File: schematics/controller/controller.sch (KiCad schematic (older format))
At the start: 11 parts, among them J1001 Screw_Terminal_01x03, J1002 Screw_Terminal_01x03, J1003 Conn_01x02_Male, J1004 Conn_01x04_Male, J1005 Screw_Terminal_01x02, J1006 Screw_Terminal_01x02, J1007 Conn_01x04_Male, J1008 Screw_Terminal_01x02, J1009 FRONTPANEL, J1010 Screw_Terminal_01x02, U1001 Module: surgeprot.mains.275.5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

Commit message: Redesign, signalling.
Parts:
- added J1010: SENS_INSIDE, symbol Screw_Terminal_01x02
- added J1011: SENS_OUTSIDE, symbol Screw_Terminal_01x02
- J1005: value Screw_Terminal_01x02 -> SENS_INSIDE
- J1006: value Screw_Terminal_01x02 -> SENS_OUTSIDE
- J1008: value Screw_Terminal_01x02 -> HEAT_VALVE
- J1012: renamed from J1010; value Screw_Terminal_01x02 -> HEAT_VALVE
- U1001: footprint (none) -> fan-controller_parts:MOV_Surge_Protector
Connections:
- net comms/SIG_X_OUT: now also J1010.1 (Pin_1), J1011.1 (Pin_1)
- net comms/SIG_Y_OUT: now also J1010.2 (Pin_2), J1011.2 (Pin_2)
- net cpu/SCL_HIBAUD renamed cpu/CPU_HIBAUD_SCL
- net cpu/SDA_HIBAUD renamed cpu/CPU_HIBAUD_SDA
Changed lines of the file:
@@
 $Descr A3 16535 11693
 encoding utf-8
-Sheet 1 21
+Sheet 1 19
 Title "Controller"
 Date "2017-09-24"
@@
 F 0 "U1001" H 3950 2450 60  0000 C CNN
 F 1 "Module: surgeprot.mains.275.5.01" H 3950 2350 39  0000 C CNN
-F 2 "" H 3950 1800 60  0000 C CNN
+F 2 "fan-controller_parts:MOV_Surge_Protector" H 3950 1500 60  0001 C CNN
 F 3 "" H 3950 1800 60  0000 C CNN
 	1    3950 2150
@@
 F3 "GND" I L 9550 9250 60
 F4 "VEE" I L 9550 9350 60
-F5 "UNMUTE_15K" I L 9550 8450 60
-F6 "UNMUTE_25K" I L 9550 8550 60
-F7 "OUT_15K_PRESENT" O R 11800 8450 60
-F8 "OUT_25K_PRESENT" O R 11800 8550 60
-F9 "EARTH" U L 9550 8950 60
-F10 "SIG_X_OUT" B R 11800 9250 60
-F11 "SIG_Y_OUT" B R 11800 9350 60
+F5 "OSC_15K_UNMUTE_10BAUD_SDA" I L 9550 8450 60
+F6 "OSC_25K_UNMUTE_10BAUD_SCL" I L 9550 8550 60
+F7 "EARTH" U L 9550 8950 60
+F8 "SIG_X_OUT" B R 11800 9250 60
+F9 "SIG_Y_OUT" B R 11800 9350 60
+F10 "DETECTOR_15K_10BAUD_SDA" O R 11800 8750 60
 $EndSheet
 $Comp
-L Screw_Terminal_01x02 J1010
+L Screw_Terminal_01x02 J1012
 U 1 1 5A4979A3
 P 15150 9250
-F 0 "J1010" H 15150 9350 50  0000 C CNN
-F 1 "Screw_Terminal_01x02" H 15150 9050 50  0001 C CNN
+F 0 "J1012" H 15150 9350 50  0000 C CNN
+F 1 "HEAT_VALVE" H 15350 9200 50  0000 L CNN
 F 2 "" H 15150 9250 50  0001 C CNN
 F 3 "" H 15150 9250 50  0001 C CNN
@@
 P 15150 3300
 F 0 "J1005" H 15150 3400 50  0000 C CNN
-F 1 "Screw_Terminal_01x02" H 15150 3100 50  0001 C CNN
+F 1 "SENS_INSIDE" H 15350 3250 50  0000 L CNN
 F 2 "" H 15150 3300 50  0001 C CNN
 F 3 "" H 15150 3300 50  0001 C CNN
@@
 P 15150 3650
 F 0 "J1006" H 15150 3750 50  0000 C CNN
-F 1 "Screw_Terminal_01x02" H 15150 3450 50  0001 C CNN
+F 1 "SENS_OUTSIDE" H 15350 3600 50  0000 L CNN
 F 2 "" H 15150 3650 50  0001 C CNN
 F 3 "" H 15150 3650 50  0001 C CNN
@@
 P 15150 4000
 F 0 "J1008" H 15150 4100 50  0000 C CNN
-F 1 "Screw_Terminal_01x02" H 15150 3800 50  0001 C CNN
+F 1 "HEAT_VALVE" H 15350 3950 50  0000 L CNN
 F 2 "" H 15150 4000 50  0001 C CNN
 F 3 "" H 15150 4000 50  0001 C CNN
@@
 F2 "V_LOGIC" U L 9550 5750 60
 F3 "GND" U L 9550 5850 60
-F4 "SDA_10" B R 11800 5450 60
-F5 "SCL_10" B R 11800 5550 60
-F6 "SDA_HIBAUD" B R 11800 5050 60
-F7 "SCL_HIBAUD" B R 11800 5150 60
+F4 "CPU_10BAUD_SDA" B R 11800 5450 60
+F5 "CPU_10BAUD_SCL" O R 11800 5550 60
+F6 "CPU_HIBAUD_SDA" B R 11800 5050 60
+F7 "CPU_HIBAUD_SCL" O R 11800 5150 60
 F8 "RESET" I R 11800 5250 60
-F9 "WR_EN" O R 11800 5650 60
+F9 "CPU_10BAUD_WR_EN" O R 11800 5650 60
 F10 "FAN_ON" O R 11800 4950 60
-$EndSheet
-$Sheet
-S 9550 6600 2250 1100
-U 5A9355B1
-F0 "comms_router" 60
-F1 "sub_assy/comms/router.sch" 60
-F2 "SCL" B R 11800 6750 60
-F3 "SDA" B R 11800 6650 60
-F4 "WR_EN" I R 11800 6850 60
-F5 "DETECTOR_15K" I R 11800 7100 60
-F6 "DETECTOR_25K" I R 11800 7200 60
-F7 "UNMUTE_15K" O L 9550 7100 60
-F8 "UNMUTE_25K" O L 9550 7200 60
-F9 "V_LOGIC" U L 9550 7550 60
-F10 "GND" U L 9550 7650 60
 $EndSheet
 $Comp
@@
 P 15150 5050
 F 0 "J1009" H 15150 5350 50  0000 C CNN
-F 1 "FRONTPANEL" H 14750 5050 50  0000 C CNN
+F 1 "FRONTPANEL" H 14500 5050 50  0000 L CNN
 F 2 "" H 15150 5050 50  0001 C CNN
 F 3 "" H 15150 5050 50  0001 C CNN
@@
 Connection ~ 14300 3750
 Wire Wire Line
-	11800 7100 12250 7100
-Wire Wire Line
-	12250 7100 12250 8450
-Wire Wire Line
-	12250 8450 11800 8450
-Wire Wire Line
-	11800 7200 12150 7200
-Wire Wire Line
-	12150 7200 12150 8550
-Wire Wire Line
-	12150 8550 11800 8550
-Wire Wire Line
-	9550 7100 9050 7100
-Wire Wire Line
-	9050 7100 9050 8450
-Wire Wire Line
-	9050 8450 9550 8450
-Wire Wire Line
-	9550 7200 9200 7200
-Wire Wire Line
-	9200 7200 9200 8550
-Wire Wire Line
-	9200 8550 9550 8550
-Wire Wire Line
 	5500 4500 14400 4500
 Wire Wire Line
@@
 	11800 5250 14950 5250
 Wire Wire Line
-	11800 5450 12250 5450
-Wire Wire Line
-	12250 5450 12250 6650
-Wire Wire Line
-	12250 6650 11800 6650
-Wire Wire Line
-	11800 5550 12150 5550
-Wire Wire Line
-	12150 5550 12150 6750
-Wire Wire Line
-	12150 6750 11800 6750
-Wire Wire Line
-	11800 5650 12050 5650
-Wire Wire Line
-	12050 5650 12050 6850
-Wire Wire Line
-	12050 6850 11800 6850
-Wire Wire Line
 	1700 10500 1700 10300
+$Sheet
+S 9550 6600 2250 1100
+U 5A9355B1
+F0 "comms_router" 60
+F1 "sub_assy/comms/router.sch" 60
+F2 "V_LOGIC" U L 9550 7550 60
+F3 "GND" U L 9550 7650 60
+F4 "OSC_25K_UNMUTE_10BAUD_SCL" O L 9550 6750 60
+F5 "CPU_10BAUD_SCL" I R 11800 7100 60
+F6 "CPU_10BAUD_WR_EN" I R 11800 7200 60
+F7 "DETECTOR_15K_10BAUD_SDA" I R 11800 7550 60
+F8 "OSC_15K_UNMUTE_10BAUD_SDA" O L 9550 6650 60
+F9 "CPU_10BAUD_SDA" B R 11800 7000 60
+$EndSheet
+Wire Wire Line
+	11800 5450 12200 5450
+Wire Wire Line
+	11800 5550 12300 5550
+Wire Wire Line
+	11800 5650 12400 5650
+Wire Wire Line
+	9300 8450 9550 8450
+Wire Wire Line
+	9200 8550 9550 8550
+Wire Wire Line
+	12400 5650 12400 7200
+Wire Wire Line
+	12400 7200 11800 7200
+Wire Wire Line
+	12300 5550 12300 7100
+Wire Wire Line
+	12300 7100 11800 7100
+Wire Wire Line
+	12200 5450 12200 7000
+Wire Wire Line
+	12200 7000 11800 7000
+Wire Wire Line
+	9550 6650 9300 6650
+Wire Wire Line
+	9300 6650 9300 8450
+Wire Wire Line
+	9550 6750 9200 6750
+Wire Wire Line
+	9200 6750 9200 8550
+Wire Wire Line
+	11800 8750 12200 8750
+Wire Wire Line
+	12200 8750 12200 7550
+Wire Wire Line
+	12200 7550 11800 7550
+$Comp
+L Screw_Terminal_01x02 J1011
+U 1 1 5B48450F
+P 15150 8700
+F 0 "J1011" H 15150 8800 50  0000 C CNN
+F 1 "SENS_OUTSIDE" H 15350 8650 50  0000 L CNN
+F 2 "" H 15150 8700 50  0001 C CNN
+F 3 "" H 15150 8700 50  0001 C CNN
+	1    15150 8700
+	1    0    0    -1
+$EndComp
+$Comp
+L Screw_Terminal_01x02 J1010
+U 1 1 5B4846AD
+P 15150 8150
+F 0 "J1010" H 15150 8250 50  0000 C CNN
+F 1 "SENS_INSIDE" H 15350 8100 50  0000 L CNN
+F 2 "" H 15150 8150 50  0001 C CNN
+F 3 "" H 15150 8150 50  0001 C CNN
+	1    15150 8150
+	1    0    0    -1
+$EndComp
+Wire Wire Line
+	14300 9350 14300 8250
+Wire Wire Line
+	14300 8250 14950 8250
+Connection ~ 14300 9350
+Wire Wire Line
+	14400 9250 14400 8150
+Wire Wire Line
+	14400 8150 14950 8150
+Connection ~ 14400 9250
+Wire Wire Line
+	14950 8800 14300 8800
+Connection ~ 14300 8800
+Wire Wire Line
+	14950 8700 14400 8700
+Connection ~ 14400 8700
 $EndSCHEMATC

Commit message: Revisions and simplifications
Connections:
- net fan-switch/N: now also J1003.1 (Pin_1); no longer J1003.2 (Pin_2)
- net at U1001.3 (LProt): now also J1003.2 (Pin_2); no longer J1003.1 (Pin_1)
- net comms/SIG_X_OUT renamed comms/SIG_X_OUTSIDE
- net comms/SIG_Y_OUT renamed comms/SIG_Y_OUTSIDE
- net dcdc_surge-prot/V_DCDC_+18_OUT renamed psu/V_DCDC_+18
- net dcdc_surge-prot/V_DCDC_0_OUT renamed psu/V_DCDC_0
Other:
- moved on the sheet: J1003

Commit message: Diagram cleanup and corrections.
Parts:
- removed J1005, J1010: SENS_INSIDE, symbol Screw_Terminal_01x02
- removed J1006, J1011: SENS_OUTSIDE, symbol Screw_Terminal_01x02
- removed J1008, J1012: HEAT_VALVE, symbol Screw_Terminal_01x02
- added D1001, D1002, D1003, D1004, D1005, D1006, D1007, D1008, D1009: 1.5KE33CA, symbol D_TVS
- added D1010, D1011, D1012, D1013, D1014, D1015, D1016, D1017, D1018: 1.5KE30CA, symbol D_TVS
- added F1001, F1002, F1003, F1004, F1005, F1006: 250mAF, symbol Fuse
- added F1007, F1008, F1009, F1010, F1011, F1012: 100mAF, symbol Fuse
- added J1003: Periphery, symbol Screw_Terminal_01x12
- added R1001, R1002, R1003, R1004, R1005, R1006: 27Ω / 1W, symbol R
- added U1002, U1003, U1004: TDK T90-A75XSMD, symbol GDT-3
- renumbered J1003 to J1004, J1004 to J1005, J1007 to J1006, J1009 to J1007
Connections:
- net comms/GND is gone; now on net cpu/CPU_HIBAUD_SCL: J1007.1 (Pin_1)
- net Earth: now also J1007.5 (Pin_5), D1001.1 (A1), D1003.1 (A1), D1004.1 (A1), D1006.1 (A1), D1007.1 (A1), D1009.1 (A1), D1010.1 (A1), D1012.1 (A1), D1013.1 (A1), D1015.1 (A1), D1016.1 (A1), D1018.1 (A1), U1002.2, U1003.2, U1004.2
- net comms_router/V_LOGIC: now also J1007.4 (Pin_4); no longer J1007.2 (Pin_2)
- net cpu/CPU_HIBAUD_SCL: no longer J1007.4 (Pin_4)
- net cpu/CPU_HIBAUD_SDA: now also J1007.2 (Pin_2); no longer J1007.3 (Pin_3)
- net cpu/RESET: now also J1007.3 (Pin_3); no longer J1007.5 (Pin_5)
- net psu/V_DCDC_+18: now also D1001.2 (A2), D1002.2 (A2), D1004.2 (A2), D1005.2 (A2), D1007.2 (A2), D1008.2 (A2), F1001.1, F1003.1, F1005.1
- net psu/V_DCDC_0: now also D1002.1 (A1), D1003.2 (A2), D1005.1 (A1), D1006.2 (A2), D1008.1 (A1), D1009.2 (A2), F1002.1, F1004.1, F1006.1
- new net: F1001.2, J1003.1 (Pin_1)
- new net: F1006.2, J1003.10 (Pin_10)
- new net: F1011.2, J1003.11 (Pin_11)
- new net: F1012.2, J1003.12 (Pin_12)
- new net: F1002.2, J1003.2 (Pin_2)
- new net: F1007.2, J1003.3 (Pin_3)
- new net: F1008.2, J1003.4 (Pin_4)
- new net: F1003.2, J1003.5 (Pin_5)
- new net: F1004.2, J1003.6 (Pin_6)
- new net: F1009.2, J1003.7 (Pin_7)
- new net: F1010.2, J1003.8 (Pin_8)
- new net: F1005.2, J1003.9 (Pin_9)
- new net: F1007.1, R1001.2, U1002.1
- new net: F1008.1, R1002.2, U1002.3
- new net: F1009.1, R1003.2, U1003.1
- new net: F1010.1, R1004.2, U1003.3
- new net: F1011.1, R1005.2, U1004.1
- new net: F1012.1, R1006.2, U1004.3
- new net comms/X: D1010.2 (A2), D1011.2 (A2), D1013.2 (A2), D1014.2 (A2), D1016.2 (A2), D1017.2 (A2), R1001.1, R1003.1, R1005.1
- new net comms/Y: D1011.1 (A1), D1012.2 (A2), D1014.1 (A1), D1015.2 (A2), D1017.1 (A1), D1018.2 (A2), R1002.1, R1004.1, R1006.1
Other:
- note added: "+18V"
- note added: "+5V"
- note added: "0V"
- note added: "FRONT_PANEL"
- note added: "HEAT_VALVE"
- note added: "RESET"
- note added: "SCL"
- note added: "SDA"
- note added: "SENS_INSIDE"
- note added: "SENS_OUTSIDE"
- note added: "Spark protector:\n TDK T90-A75XSMD\n Sparkover voltage: 75V +/- 20%"
- note added: "X"
- note added: "Y"
- moved on the sheet: J1001, J1002, J1004, J1005, J1006, J1007, U1001

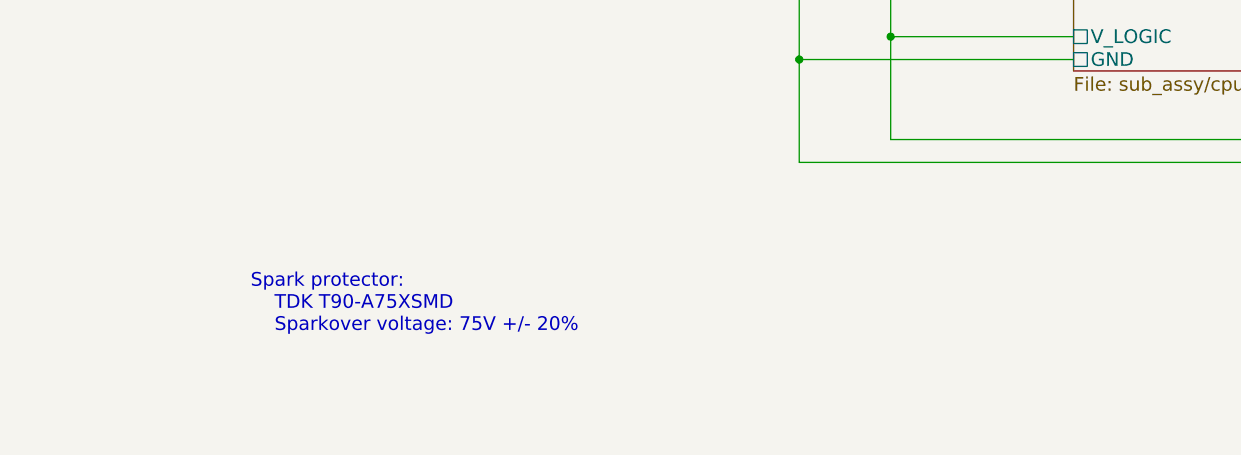
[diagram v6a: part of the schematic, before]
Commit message: Creating BOM (with ordering)
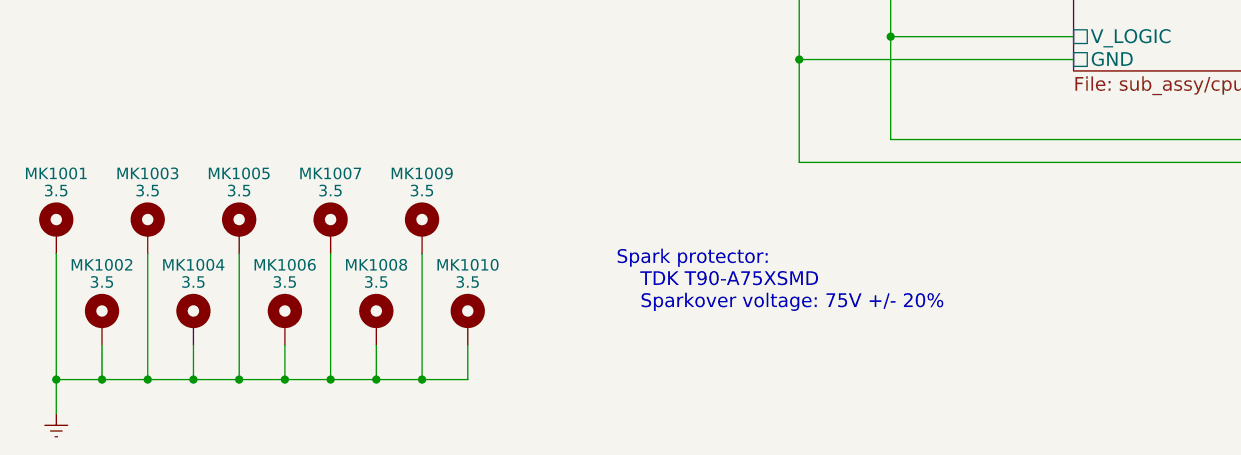
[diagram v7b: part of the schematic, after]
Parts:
- added MK1001, MK1002, MK1003, MK1004, MK1005, MK1006, MK1007, MK1008, MK1009, MK1010: 3.5, symbol Mounting_Hole_PAD
- U1001: footprint fan-controller_parts:MOV_Surge_Protector -> (none)
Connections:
- net Earth: now also MK1001.1, MK1002.1, MK1003.1, MK1004.1, MK1005.1, MK1006.1, MK1007.1, MK1008.1, MK1009.1, MK1010.1
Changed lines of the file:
@@
 F 0 "U1001" H 3000 2450 60  0000 C CNN
 F 1 "Module: surgeprot.mains.275.5.01" H 3000 2350 39  0000 C CNN
-F 2 "fan-controller_parts:MOV_Surge_Protector" H 3000 1500 60  0001 C CNN
+F 2 "" H 3000 1500 60  0001 C CNN
 F 3 "" H 3000 1800 60  0000 C CNN
 	1    3000 2150
@@
 	0    -1   -1   0
 $EndComp
-Text Notes 1750 10450 0    60   ~ 0
+Text Notes 3350 10350 0    60   ~ 0
 Spark protector:\n    TDK T90-A75XSMD\n    Sparkover voltage: 75V +/- 20%
 Wire Wire Line
@@
 	14350 9350 14600 9350
 Connection ~ 10150 9700
+$Comp
+L Mounting_Hole_PAD MK1005
+U 1 1 5B5F91C5
+P 1700 10000
+F 0 "MK1005" H 1700 10250 50  0000 C CNN
+F 1 "3.5" H 1700 10175 50  0000 C CNN
+F 2 "" H 1700 10000 50  0001 C CNN
+F 3 "" H 1700 10000 50  0001 C CNN
+	1    1700 10000
+	1    0    0    -1
+$EndComp
+$Comp
+L Mounting_Hole_PAD MK1006
+U 1 1 5B5FD13B
+P 1900 10400
+F 0 "MK1006" H 1900 10650 50  0000 C CNN
+F 1 "3.5" H 1900 10575 50  0000 C CNN
+F 2 "" H 1900 10400 50  0001 C CNN
+F 3 "" H 1900 10400 50  0001 C CNN
+	1    1900 10400
+	1    0    0    -1
+$EndComp
+$Comp
+L Mounting_Hole_PAD MK1007
+U 1 1 5B5FD551
+P 2100 10000
+F 0 "MK1007" H 2100 10250 50  0000 C CNN
+F 1 "3.5" H 2100 10175 50  0000 C CNN
+F 2 "" H 2100 10000 50  0001 C CNN
+F 3 "" H 2100 10000 50  0001 C CNN
+	1    2100 10000
+	1    0    0    -1
+$EndComp
+$Comp
+L Mounting_Hole_PAD MK1008
+U 1 1 5B5FD557
+P 2300 10400
+F 0 "MK1008" H 2300 10650 50  0000 C CNN
+F 1 "3.5" H 2300 10575 50  0000 C CNN
+F 2 "" H 2300 10400 50  0001 C CNN
+F 3 "" H 2300 10400 50  0001 C CNN
+	1    2300 10400
+	1    0    0    -1
+$EndComp
+$Comp
+L Mounting_Hole_PAD MK1001
+U 1 1 5B5FDB23
+P 900 10000
+F 0 "MK1001" H 900 10250 50  0000 C CNN
+F 1 "3.5" H 900 10175 50  0000 C CNN
+F 2 "" H 900 10000 50  0001 C CNN
+F 3 "" H 900 10000 50  0001 C CNN
+	1    900  10000
+	1    0    0    -1
+$EndComp
+$Comp
+L Mounting_Hole_PAD MK1002
+U 1 1 5B5FDB29
+P 1100 10400
+F 0 "MK1002" H 1100 10650 50  0000 C CNN
+F 1 "3.5" H 1100 10575 50  0000 C CNN
+F 2 "" H 1100 10400 50  0001 C CNN
+F 3 "" H 1100 10400 50  0001 C CNN
+	1    1100 10400
+	1    0    0    -1
+$EndComp
+$Comp
+L Mounting_Hole_PAD MK1003
+U 1 1 5B5FDB2F
+P 1300 10000
+F 0 "MK1003" H 1300 10250 50  0000 C CNN
+F 1 "3.5" H 1300 10175 50  0000 C CNN
+F 2 "" H 1300 10000 50  0001 C CNN
+F 3 "" H 1300 10000 50  0001 C CNN
+	1    1300 10000
+	1    0    0    -1
+$EndComp
+$Comp
+L Mounting_Hole_PAD MK1004
+U 1 1 5B5FDB35
+P 1500 10400
+F 0 "MK1004" H 1500 10650 50  0000 C CNN
+F 1 "3.5" H 1500 10575 50  0000 C CNN
+F 2 "" H 1500 10400 50  0001 C CNN
+F 3 "" H 1500 10400 50  0001 C CNN
+	1    1500 10400
+	1    0    0    -1
+$EndComp
+$Comp
+L Mounting_Hole_PAD MK1009
+U 1 1 5B5FDEA3
+P 2500 10000
+F 0 "MK1009" H 2500 10250 50  0000 C CNN
+F 1 "3.5" H 2500 10175 50  0000 C CNN
+F 2 "" H 2500 10000 50  0001 C CNN
+F 3 "" H 2500 10000 50  0001 C CNN
+	1    2500 10000
+	1    0    0    -1
+$EndComp
+$Comp
+L Mounting_Hole_PAD MK1010
+U 1 1 5B5FDEA9
+P 2700 10400
+F 0 "MK1010" H 2700 10650 50  0000 C CNN
+F 1 "3.5" H 2700 10575 50  0000 C CNN
+F 2 "" H 2700 10400 50  0001 C CNN
+F 3 "" H 2700 10400 50  0001 C CNN
+	1    2700 10400
+	1    0    0    -1
+$EndComp
+$Comp
+L Earth #PWR02
+U 1 1 5B602CCF
+P 900 10800
+F 0 "#PWR02" H 900 10550 50  0001 C CNN
+F 1 "Earth" H 900 10650 50  0001 C CNN
+F 2 "" H 900 10800 50  0001 C CNN
+F 3 "" H 900 10800 50  0001 C CNN
+	1    900  10800
+	1    0    0    -1
+$EndComp
+Wire Wire Line
+	900  10100 900  10800
+Wire Wire Line
+	1100 10500 1100 10650
+Wire Wire Line
+	900  10650 2700 10650
+Connection ~ 900  10650
+Wire Wire Line
+	1300 10650 1300 10100
+Connection ~ 1100 10650
+Wire Wire Line
+	1500 10650 1500 10500
+Connection ~ 1300 10650
+Wire Wire Line
+	1700 10650 1700 10100
+Connection ~ 1500 10650
+Wire Wire Line
+	1900 10650 1900 10500
+Connection ~ 1700 10650
+Wire Wire Line
+	2100 10650 2100 10100
+Connection ~ 1900 10650
+Wire Wire Line
+	2300 10650 2300 10500
+Connection ~ 2100 10650
+Wire Wire Line
+	2500 10650 2500 10100
+Connection ~ 2300 10650
+Wire Wire Line
+	2700 10650 2700 10500
+Connection ~ 2500 10650
 $EndSCHEMATC

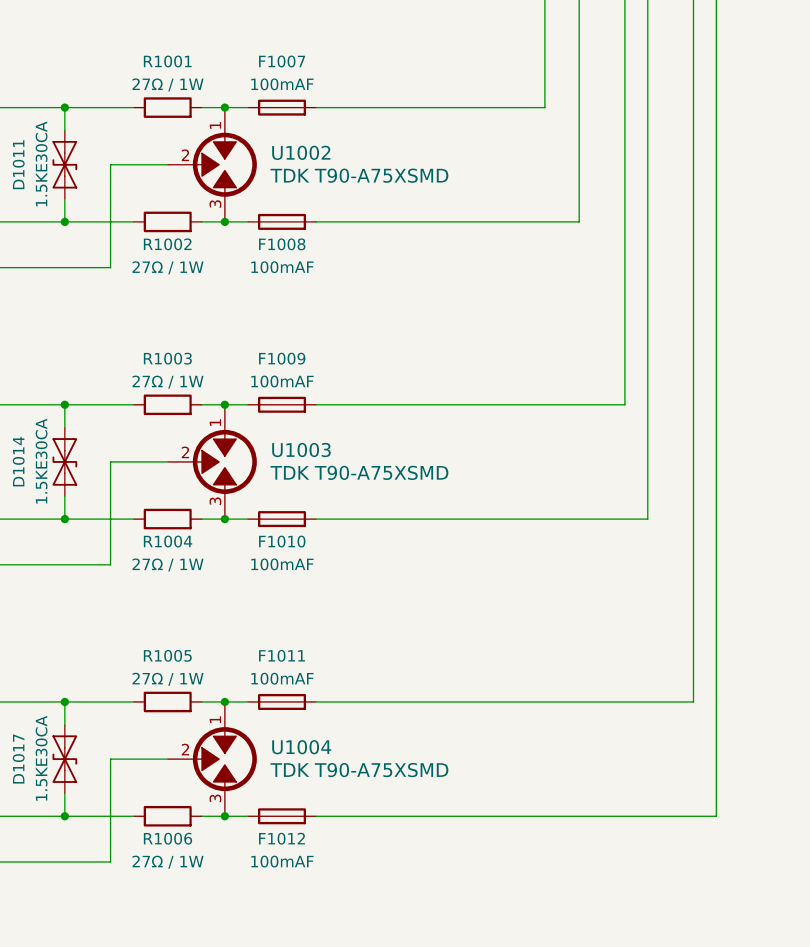
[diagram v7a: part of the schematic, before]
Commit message: Controller: Assigned footprints. Designing PCB.
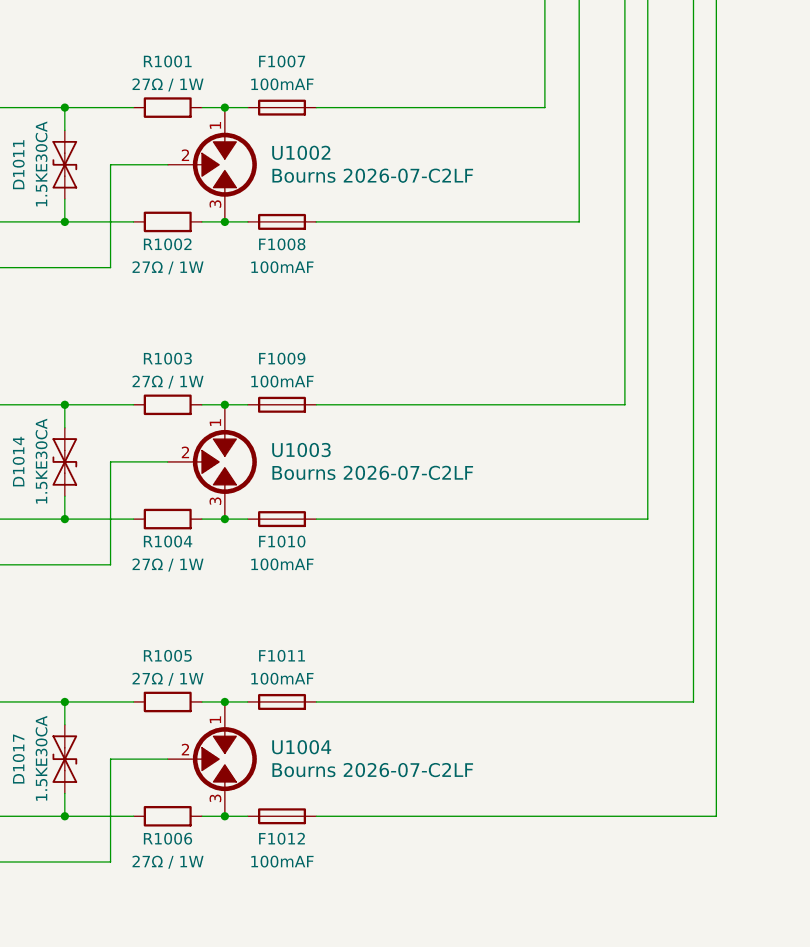
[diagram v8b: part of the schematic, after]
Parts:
- D1001, D1002, D1003, D1004, D1005, D1006, D1007, D1008, D1009, D1010, D1011, D1012, D1013, D1014, D1015, D1016, D1017, D1018: footprint (none) -> Diodes_THT:D_DO-201AD_P12.70mm_Horizontal
- F1001, F1002, F1003, F1004, F1005, F1006, F1007, F1008, F1009, F1010, F1011, F1012: footprint (none) -> Fuse_Holders_and_Fuses:Fuseholder5x20_horiz_open_Schurter_0031_8201
- J1001, J1002: footprint (none) -> Connectors_Phoenix:PhoenixContact_MSTBVA-G_03x5.00mm_Vertical
- J1003: footprint (none) -> Connectors_Phoenix:PhoenixContact_MSTBVA-G_12x5.00mm_Vertical
- J1004: footprint (none) -> footprints:TE_1969799-1
- J1005, J1006: footprint (none) -> footprints:TE_1969807-1
- J1007: footprint (none) -> Pin_Headers:Pin_Header_Straight_1x05_Pitch2.54mm
- MK1001, MK1002, MK1003, MK1004, MK1005, MK1006, MK1007, MK1008, MK1009, MK1010: footprint (none) -> Mounting_Holes:MountingHole_3.5mm_Pad_Via
- R1001, R1002, R1003, R1004, R1005, R1006: footprint (none) -> Resistors_THT:R_Axial_DIN0414_L11.9mm_D4.5mm_P15.24mm_Horizontal
- U1001: footprint (none) -> footprints:TE_1969803-1
- U1002, U1003, U1004: value TDK T90-A75XSMD -> Bourns 2026-07-C2LF; footprint (none) -> footprints:Bourns_2026-xx
